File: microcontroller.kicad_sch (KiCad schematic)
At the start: 11 parts, among them U4 ESP32-S3-WROOM-1, Y41 Crystal

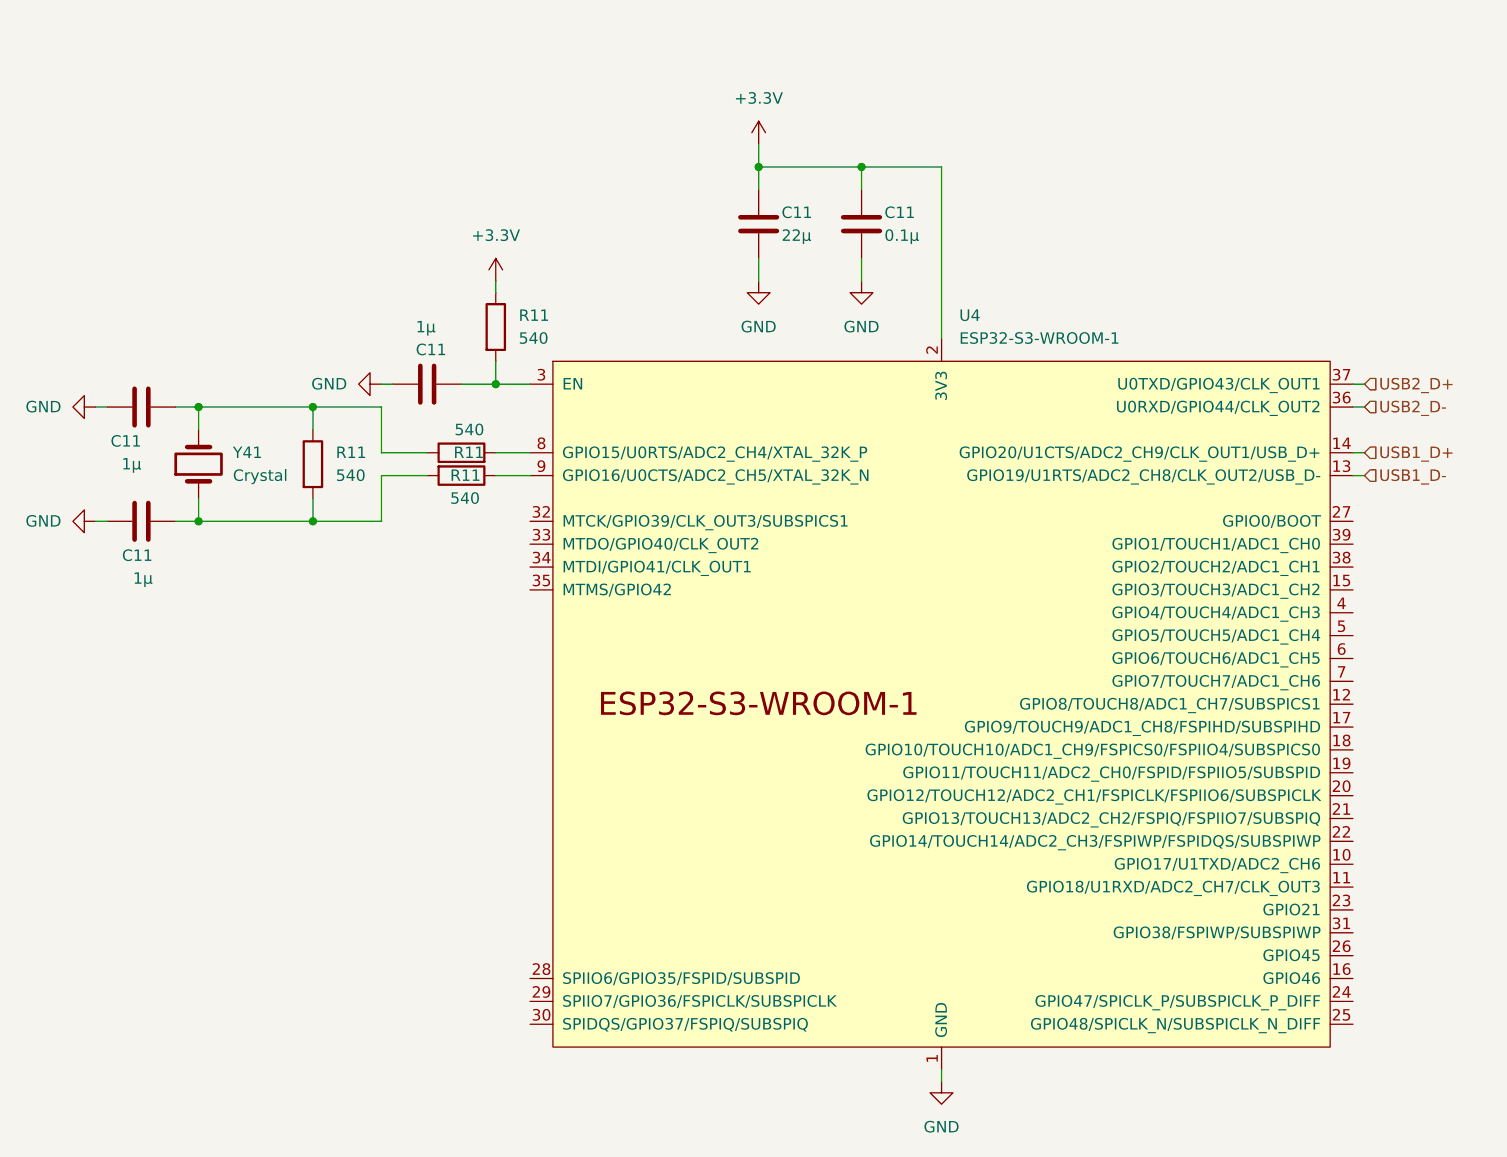
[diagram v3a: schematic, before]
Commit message: completed ESP32-S3 circuit
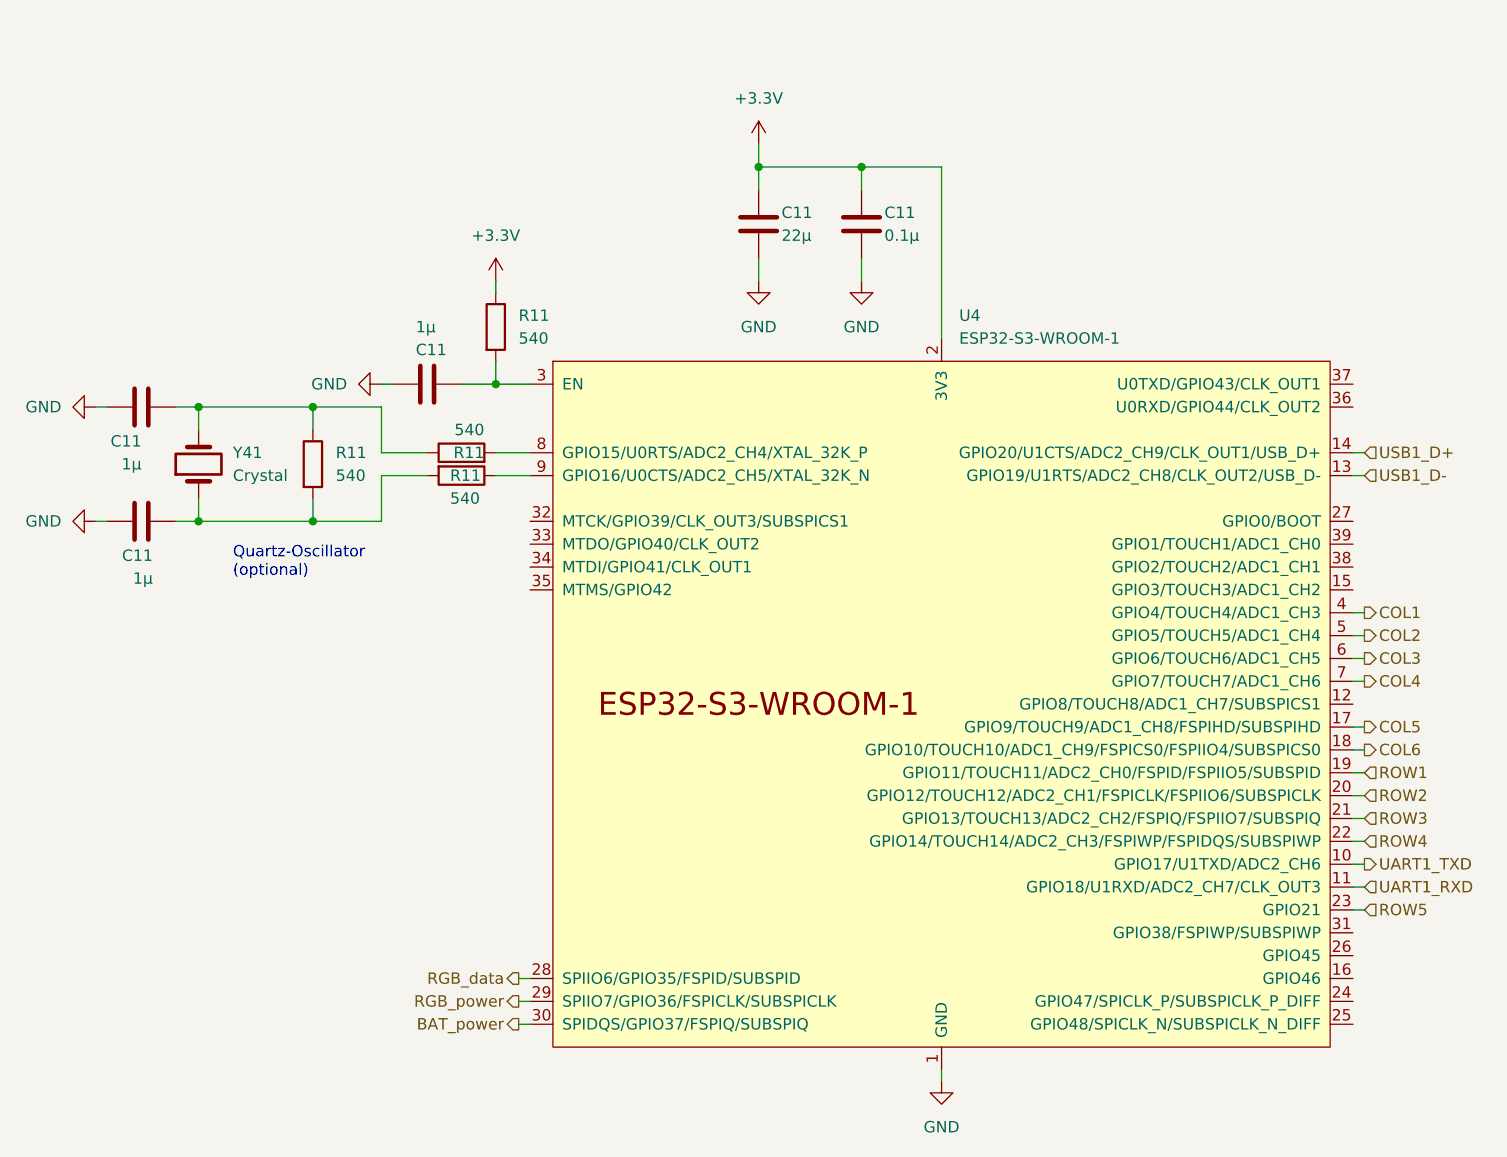
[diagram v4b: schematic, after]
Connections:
- net UART1_TXD: now reaches U4.10 (GPIO17/U1TXD/ADC2_CH6)
- net UART1_RXD: now reaches U4.11 (GPIO18/U1RXD/ADC2_CH7/CLK_OUT3)
- net COL5: now reaches U4.17 (GPIO9/TOUCH9/ADC1_CH8/FSPIHD/SUBSPIHD)
- net COL6: now reaches U4.18 (GPIO10/TOUCH10/ADC1_CH9/FSPICS0/FSPIIO4/SUBSPICS0)
- net ROW1: now reaches U4.19 (GPIO11/TOUCH11/ADC2_CH0/FSPID/FSPIIO5/SUBSPID)
- net ROW2: now reaches U4.20 (GPIO12/TOUCH12/ADC2_CH1/FSPICLK/FSPIIO6/SUBSPICLK)
- net ROW3: now reaches U4.21 (GPIO13/TOUCH13/ADC2_CH2/FSPIQ/FSPIIO7/SUBSPIQ)
- net ROW4: now reaches U4.22 (GPIO14/TOUCH14/ADC2_CH3/FSPIWP/FSPIDQS/SUBSPIWP)
- net ROW5: now reaches U4.23 (GPIO21)
- net RGB_data: now reaches U4.28 (SPIIO6/GPIO35/FSPID/SUBSPID)
- net RGB_power: now reaches U4.29 (SPIIO7/GPIO36/FSPICLK/SUBSPICLK)
- net BAT_power: now reaches U4.30 (SPIDQS/GPIO37/FSPIQ/SUBSPIQ)
- net COL1: now reaches U4.4 (GPIO4/TOUCH4/ADC1_CH3)
- net COL2: now reaches U4.5 (GPIO5/TOUCH5/ADC1_CH4)
- net COL3: now reaches U4.6 (GPIO6/TOUCH6/ADC1_CH5)
- net COL4: now reaches U4.7 (GPIO7/TOUCH7/ADC1_CH6)
- net USB2_D+: no longer names the net of U4.37 (U0TXD/GPIO43/CLK_OUT1)
- net USB2_D-: no longer names the net of U4.36 (U0RXD/GPIO44/CLK_OUT2)
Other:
- note added: "Quartz-Oscillator (optional)"
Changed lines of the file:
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@@
   (junction (at 77.47 74.93) (diameter 0) (color 0 0 0 0)
   )
+  (wire (pts (xy 80.01 140.97) (xy 81.28 140.97))
+    (stroke (width 0) (type default))
+  )
   (wire (pts (xy 127 152.4) (xy 127 151.13))
     (stroke (width 0) (type default))
@@
     (stroke (width 0) (type default))
   )
+  (wire (pts (xy 173.99 128.27) (xy 172.72 128.27))
+    (stroke (width 0) (type default))
+  )
   (wire (pts (xy 64.77 82.55) (xy 69.85 82.55))
     (stroke (width 0) (type default))
@@
     (stroke (width 0) (type default))
   )
+  (wire (pts (xy 173.99 113.03) (xy 172.72 113.03))
+    (stroke (width 0) (type default))
+  )
+  (wire (pts (xy 173.99 115.57) (xy 172.72 115.57))
+    (stroke (width 0) (type default))
+  )
+  (wire (pts (xy 173.99 120.65) (xy 172.72 120.65))
+    (stroke (width 0) (type default))
+  )
+  (wire (pts (xy 173.99 102.87) (xy 172.72 102.87))
+    (stroke (width 0) (type default))
+  )
   (wire (pts (xy 57.15 77.47) (xy 44.45 77.47))
     (stroke (width 0) (type default))
@@
     (stroke (width 0) (type default))
   )
+  (wire (pts (xy 173.99 125.73) (xy 172.72 125.73))
+    (stroke (width 0) (type default))
+  )
   (wire (pts (xy 106.68 48.26) (xy 106.68 50.8))
     (stroke (width 0) (type default))
   )
+  (wire (pts (xy 80.01 146.05) (xy 81.28 146.05))
+    (stroke (width 0) (type default))
+  )
+  (wire (pts (xy 173.99 107.95) (xy 172.72 107.95))
+    (stroke (width 0) (type default))
+  )
   (wire (pts (xy 33.02 77.47) (xy 34.29 77.47))
     (stroke (width 0) (type default))
@@
     (stroke (width 0) (type default))
   )
-  (wire (pts (xy 173.99 74.93) (xy 172.72 74.93))
-    (stroke (width 0) (type default))
-  )
   (wire (pts (xy 44.45 77.47) (xy 44.45 80.01))
     (stroke (width 0) (type default))
@@
     (stroke (width 0) (type default))
   )
+  (wire (pts (xy 173.99 100.33) (xy 172.72 100.33))
+    (stroke (width 0) (type default))
+  )
   (wire (pts (xy 173.99 82.55) (xy 172.72 82.55))
     (stroke (width 0) (type default))
@@
     (stroke (width 0) (type default))
   )
+  (wire (pts (xy 173.99 133.35) (xy 172.72 133.35))
+    (stroke (width 0) (type default))
+  )
   (wire (pts (xy 77.47 74.93) (xy 81.28 74.93))
     (stroke (width 0) (type default))
   )
+  (wire (pts (xy 80.01 143.51) (xy 81.28 143.51))
+    (stroke (width 0) (type default))
+  )
   (wire (pts (xy 33.02 90.17) (xy 34.29 90.17))
     (stroke (width 0) (type default))
@@
     (stroke (width 0) (type default))
   )
-  (wire (pts (xy 173.99 77.47) (xy 172.72 77.47))
+  (wire (pts (xy 173.99 105.41) (xy 172.72 105.41))
+    (stroke (width 0) (type default))
+  )
+  (wire (pts (xy 173.99 123.19) (xy 172.72 123.19))
     (stroke (width 0) (type default))
   )
@@
     (stroke (width 0) (type default))
   )
+  (wire (pts (xy 173.99 130.81) (xy 172.72 130.81))
+    (stroke (width 0) (type default))
+  )
   (wire (pts (xy 64.77 74.93) (xy 66.04 74.93))
     (stroke (width 0) (type default))
@@
     (stroke (width 0) (type default))
   )
-  (hierarchical_label "USB2_D-" (shape input) (at 173.99 77.47 0) (fields_autoplaced)
+  (wire (pts (xy 173.99 118.11) (xy 172.72 118.11))
+    (stroke (width 0) (type default))
+  )
+  (text "Quartz-Oscillator\n(optional)" (at 48.26 96.52 0)
+    (effects (font (size 1.27 1.27)) (justify left bottom))
+  )
+  (hierarchical_label "ROW5" (shape input) (at 173.99 133.35 0) (fields_autoplaced)
+    (effects (font (size 1.27 1.27)) (justify left))
+  )
+  (hierarchical_label "COL6" (shape output) (at 173.99 115.57 0) (fields_autoplaced)
+    (effects (font (size 1.27 1.27)) (justify left))
+  )
+  (hierarchical_label "COL3" (shape output) (at 173.99 105.41 0) (fields_autoplaced)
+    (effects (font (size 1.27 1.27)) (justify left))
+  )
+  (hierarchical_label "RGB_data" (shape output) (at 80.01 140.97 180) (fields_autoplaced)
+    (effects (font (size 1.27 1.27)) (justify right))
+  )
+  (hierarchical_label "UART1_RXD" (shape input) (at 173.99 130.81 0) (fields_autoplaced)
+    (effects (font (size 1.27 1.27)) (justify left))
+  )
+  (hierarchical_label "UART1_TXD" (shape output) (at 173.99 128.27 0) (fields_autoplaced)
+    (effects (font (size 1.27 1.27)) (justify left))
+  )
+  (hierarchical_label "COL1" (shape output) (at 173.99 100.33 0) (fields_autoplaced)
+    (effects (font (size 1.27 1.27)) (justify left))
+  )
+  (hierarchical_label "COL4" (shape output) (at 173.99 107.95 0) (fields_autoplaced)
     (effects (font (size 1.27 1.27)) (justify left))
   )
@@
     (effects (font (size 1.27 1.27)) (justify left))
   )
+  (hierarchical_label "COL5" (shape output) (at 173.99 113.03 0) (fields_autoplaced)
+    (effects (font (size 1.27 1.27)) (justify left))
+  )
+  (hierarchical_label "BAT_power" (shape output) (at 80.01 146.05 180) (fields_autoplaced)
+    (effects (font (size 1.27 1.27)) (justify right))
+  )
   (hierarchical_label "USB1_D+" (shape input) (at 173.99 82.55 0) (fields_autoplaced)
     (effects (font (size 1.27 1.27)) (justify left))
   )
-  (hierarchical_label "USB2_D+" (shape input) (at 173.99 74.93 0) (fields_autoplaced)
+  (hierarchical_label "ROW4" (shape input) (at 173.99 125.73 0) (fields_autoplaced)
+    (effects (font (size 1.27 1.27)) (justify left))
+  )
+  (hierarchical_label "ROW3" (shape input) (at 173.99 123.19 0) (fields_autoplaced)
+    (effects (font (size 1.27 1.27)) (justify left))
+  )
+  (hierarchical_label "RGB_power" (shape output) (at 80.01 143.51 180) (fields_autoplaced)
+    (effects (font (size 1.27 1.27)) (justify right))
+  )
+  (hierarchical_label "COL2" (shape output) (at 173.99 102.87 0) (fields_autoplaced)
+    (effects (font (size 1.27 1.27)) (justify left))
+  )
+  (hierarchical_label "ROW1" (shape input) (at 173.99 118.11 0) (fields_autoplaced)
+    (effects (font (size 1.27 1.27)) (justify left))
+  )
+  (hierarchical_label "ROW2" (shape input) (at 173.99 120.65 0) (fields_autoplaced)
     (effects (font (size 1.27 1.27)) (justify left))
   )
@@
         )
         (path "/a0958e12-2248-4ac3-b259-3086ac296b70/e89ddc09-3400-44c0-8130-3ab15c16d278"
-          (reference "C2") (unit 1)
+          (reference "C41") (unit 1)
         )
       )
@@
         )
         (path "/a0958e12-2248-4ac3-b259-3086ac296b70/e89ddc09-3400-44c0-8130-3ab15c16d278"
-          (reference "C41") (unit 1)
+          (reference "C44") (unit 1)
         )
       )
@@
         )
         (path "/a0958e12-2248-4ac3-b259-3086ac296b70/e89ddc09-3400-44c0-8130-3ab15c16d278"
-          (reference "R5") (unit 1)
+          (reference "R41") (unit 1)
         )
       )
@@
         )
         (path "/a0958e12-2248-4ac3-b259-3086ac296b70/e89ddc09-3400-44c0-8130-3ab15c16d278"
-          (reference "C1") (unit 1)
+          (reference "C43") (unit 1)
         )
       )
@@
         )
         (path "/a0958e12-2248-4ac3-b259-3086ac296b70/e89ddc09-3400-44c0-8130-3ab15c16d278"
-          (reference "R41") (unit 1)
+          (reference "R44") (unit 1)
         )
       )
@@
         )
         (path "/a0958e12-2248-4ac3-b259-3086ac296b70/e89ddc09-3400-44c0-8130-3ab15c16d278"
-          (reference "C3") (unit 1)
+          (reference "C42") (unit 1)
         )
       )
@@
         )
         (path "/a0958e12-2248-4ac3-b259-3086ac296b70/e89ddc09-3400-44c0-8130-3ab15c16d278"
-          (reference "C42") (unit 1)
-        )
-      )
+          (reference "C45") (unit 1)
+        )
+      )

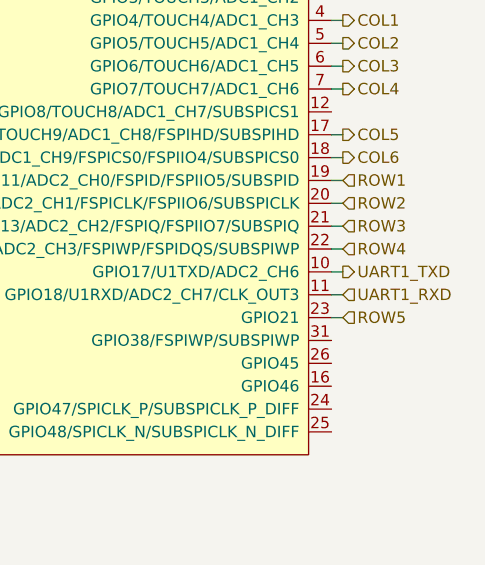
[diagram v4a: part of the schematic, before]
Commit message: switched from UART via USB-C-DAM to I2C via USB-C-AAAM
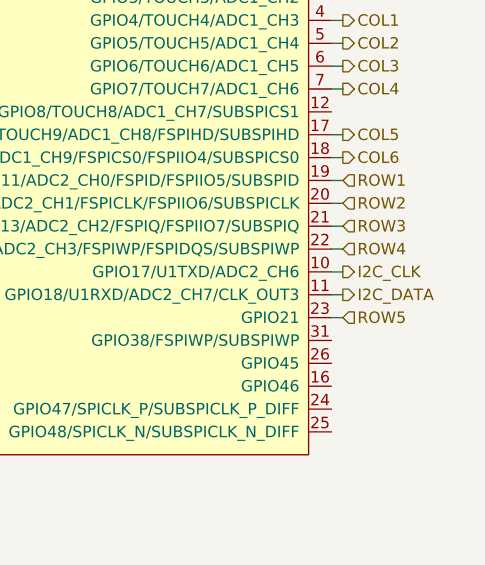
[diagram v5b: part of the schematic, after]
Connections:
- net UART1_RXD renamed I2C_DATA
- net UART1_TXD renamed I2C_CLK
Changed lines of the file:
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@@
     (effects (font (size 1.27 1.27)) (justify right))
   )
-  (hierarchical_label "UART1_RXD" (shape input) (at 173.99 130.81 0) (fields_autoplaced)
+  (hierarchical_label "I2C_DATA" (shape output) (at 173.99 130.81 0) (fields_autoplaced)
     (effects (font (size 1.27 1.27)) (justify left))
   )
-  (hierarchical_label "UART1_TXD" (shape output) (at 173.99 128.27 0) (fields_autoplaced)
+  (hierarchical_label "I2C_CLK" (shape output) (at 173.99 128.27 0) (fields_autoplaced)
     (effects (font (size 1.27 1.27)) (justify left))
   )
